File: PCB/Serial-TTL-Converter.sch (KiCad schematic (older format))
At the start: 68 parts, among them J1 RS232 (PC), J2 TTL (uC), J3 power-supply, Q1 BC817, Q2 BC817, Q3 BC817, Q4 BC817, Q5 BC817, Q6 BC817, SW1 SW_SPDT, U1 LT8570, U2 ST75185, U3 MAX736, U4 AP1117-33

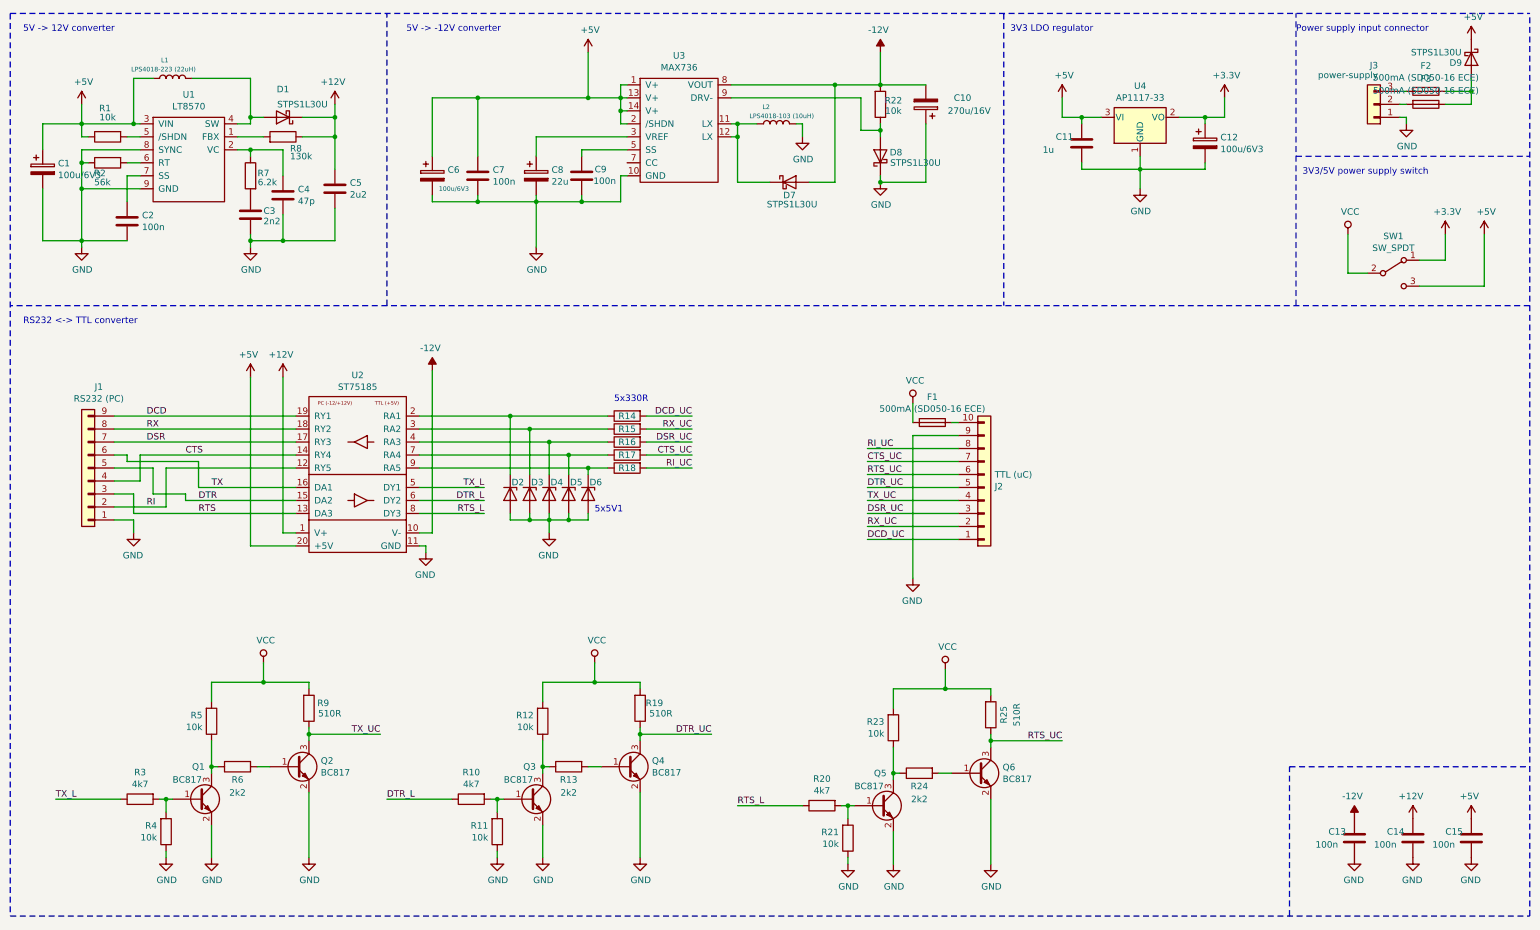
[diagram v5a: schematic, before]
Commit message: Major concept change - use MAX2323 istead of ST75185 (no need power converters)
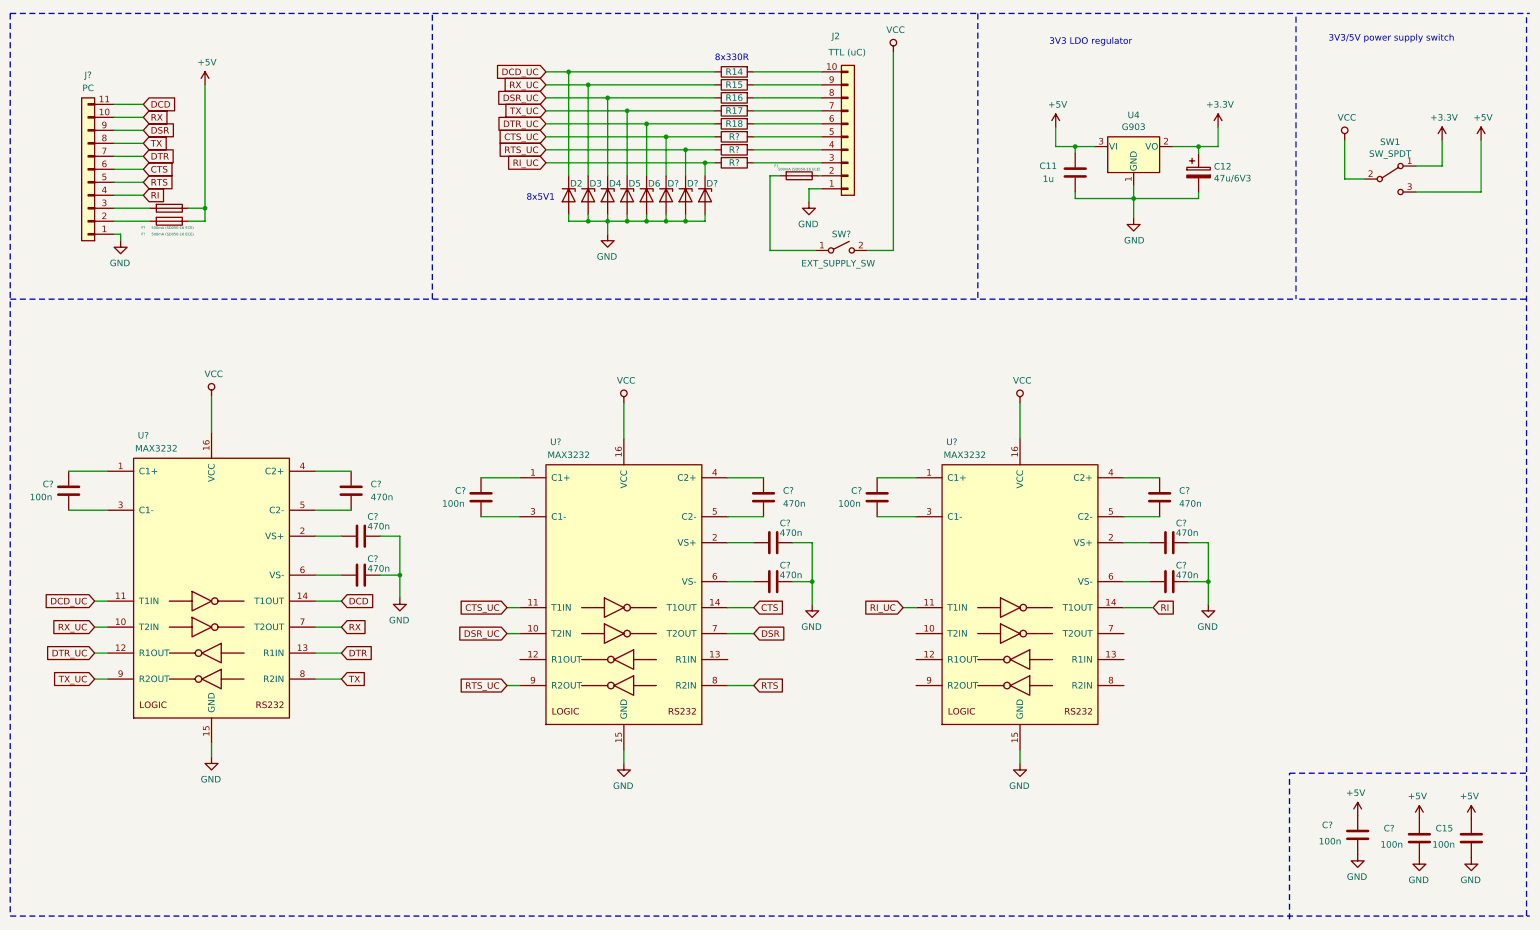
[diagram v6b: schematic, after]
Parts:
- removed C1, C6: 100u/6V3, Capacitor_THT:CP_Radial_D6.3mm_P2.50mm, symbol Device:CP
- removed C10: 270u/16V, Capacitor_THT:CP_Radial_D8.0mm_P3.50mm, symbol Device:CP
- removed C13, C14, C2, C7, C9: 100n, Capacitors_SMD:C_0805, symbol Device:C
- removed C3: 2n2, Capacitors_SMD:C_0805, symbol Device:C
- removed C4: 47p, Capacitors_SMD:C_0805, symbol Device:C
- removed C5: 2u2, Capacitors_SMD:C_0805, symbol Device:C
- removed C8: 22u, Capacitors_Tantalum_SMD:CP_Tantalum_Case-C_EIA-6032-28_Reflow, symbol Device:CP
- removed D1, D7, D8, D9: STPS1L30U, Diodes_SMD:D_SMB, symbol Device:D_Schottky
- removed F2, F3: 500mA (SD050-16 ECE), Fuse:Fuse_1812_4532Metric, symbol Device:Fuse
- removed J1: RS232 (PC), Connectors:1X09_LONGPADS, symbol Connector_Generic:Conn_01x09
- removed J3: power-supply, Connectors:1X03_LONGPADS, symbol Connector_Generic:Conn_01x03
- removed L1: LPS4018-223 (22uH), Inductor_SMD:L_Coilcraft_LPS4018, symbol Device:L
- removed L2: LPS4018-103 (10uH), Inductor_SMD:L_Coilcraft_LPS4018, symbol Device:L
- removed Q1, Q2, Q3, Q4, Q5, Q6: BC817, TO_SOT_Packages_SMD:SOT-23, symbol Transistor_BJT:BC817
- removed R1, R11, R12, R21, R22, R23, R4, R5: 10k, Resistors_SMD:R_0805, symbol Device:R
- removed R10, R20, R3: 4k7, Resistors_SMD:R_0805, symbol Device:R
- removed R13, R24, R6: 2k2, Resistors_SMD:R_0805, symbol Device:R
- removed R19, R25, R9: 510R, Resistors_SMD:R_0805, symbol Device:R
- removed R2: 56k, Resistors_SMD:R_0805, symbol Device:R
- removed R7: 6.2k, Resistors_SMD:R_0805, symbol Device:R
- removed R8: 130k, Resistors_SMD:R_0805, symbol Device:R
- removed U1: LT8570, Housings_SSOP:MSOP-8-1EP_3x3mm_Pitch0.65mm, symbol Serial-TTL-Converter-rescue:LT8570-project-symbols
- removed U2: ST75185, Housings_SOIC:SO-20_12.8x7.5mm_Pitch1.27mm, symbol Serial-TTL-Converter-rescue:ST75185-project-symbols
- removed U3: MAX736, Silicon-Standard:DIP14, symbol Serial-TTL-Converter-rescue:MAX736-project-symbols
- added C? (x5): 100n, Capacitors_SMD:C_0805, symbol Device:C
- added C? (x9): 470n, Capacitors_SMD:C_0805, symbol Device:C
- added D? (x3): 5V1, Diodes_SMD:D_MiniMELF, symbol Device:D_Zener
- added F? (x2): 500mA (SD050-16 ECE), Fuse:Fuse_1812_4532Metric, symbol Device:Fuse
- added J?: PC, symbol Connector_Generic:Conn_01x11
- added R? (x3): 330R, Resistors_SMD:R_0805, symbol Device:R
- added SW?: EXT_SUPPLY_SW, symbol Switch:SW_SPST
- added U? (x3): MAX3232, Housings_SOIC:SOIC-16_3.9x9.9mm_Pitch1.27mm, symbol Interface_UART:MAX3232
- C12: value 100u/6V3 -> 47u/6V3
- U4: value AP1117-33 -> G903; footprint TO_SOT_Packages_SMD:SOT-223 -> TO_SOT_Packages_SMD:SOT-223-3_TabPin2
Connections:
- net +5V: now also C?.1, C?.1, F?.1, F?.1
- net CTS: now also J?.6 (Pin_6), U?.14 (T1OUT)
- net CTS_UC: now also D?.1 (K), R?.1, U?.11 (T1IN); no longer J2.7 (Pin_7), R17.2
- net DCD: now also J?.11 (Pin_11), U?.14 (T1OUT)
- net DCD_UC: now also D2.1 (K), R14.1, U?.11 (T1IN); no longer J2.1 (Pin_1), R14.2
- net DSR: now also J?.9 (Pin_9), U?.7 (T2OUT)
- net DSR_UC: now also D4.1 (K), R16.1, U?.10 (T2IN); no longer J2.3 (Pin_3), R16.2
- net DTR: now also J?.7 (Pin_7), U?.13 (R1IN)
- net DTR_UC: now also D6.1 (K), R18.1, U?.12 (R1OUT); no longer J2.5 (Pin_5)
- net GND: now also J2.1 (Pin_1), C?.1, C?.1, C?.1, C?.1, C?.1, C?.1, C?.2, C?.2, D?.2 (A), D?.2 (A), D?.2 (A), J?.1 (Pin_1), U?.15 (GND), U?.15 (GND), U?.15 (GND); no longer J2.9 (Pin_9)
- net RI: now also J?.4 (Pin_4), U?.14 (T1OUT)
- net RI_UC: now also D?.1 (K), R?.1, U?.11 (T1IN); no longer J2.8 (Pin_8), R18.2
- net RTS: now also J?.5 (Pin_5), U?.8 (R2IN)
- net RTS_UC: now also D?.1 (K), R?.1, U?.9 (R2OUT); no longer J2.6 (Pin_6)
- net RX: now also J?.10 (Pin_10), U?.7 (T2OUT)
- net RX_UC: now also D3.1 (K), R15.1, U?.10 (T2IN); no longer J2.2 (Pin_2), R15.2
- net TX: now also J?.8 (Pin_8), U?.8 (R2IN)
- net TX_UC: now also D5.1 (K), R17.1, U?.9 (R2OUT); no longer J2.4 (Pin_4)
- net VCC: now also SW?.2 (B), U?.16 (VCC), U?.16 (VCC), U?.16 (VCC); no longer F1.2
- net at J2.10 (Pin_10): now also R14.2; no longer F1.1
- new net: F1.1, J2.2 (Pin_2)
- new net: J2.3 (Pin_3), R?.2
- new net: J2.4 (Pin_4), R?.2
- new net: J2.5 (Pin_5), R?.2
- new net: J2.6 (Pin_6), R18.2
- new net: J2.7 (Pin_7), R17.2
- new net: J2.8 (Pin_8), R16.2
- new net: J2.9 (Pin_9), R15.2
- new net: F1.2, SW?.1 (A)
- new net: F?.2, J?.2 (Pin_2)
- new net: F?.2, J?.3 (Pin_3)
- new net: C?.1, U?.1 (C1+) (x3)
- new net: C?.2, U?.2 (VS+) (x3)
- new net: C?.2, U?.3 (C1-) (x3)
- new net: C?.1, U?.4 (C2+) (x3)
- new net: C?.2, U?.5 (C2-) (x3)
- new net: C?.2, U?.6 (VS-) (x3)
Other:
- note added: "8x330R\n"
- note added: "8x5V1"
- note removed: "5V -> -12V converter"
- note removed: "5V -> 12V converter"
- note removed: "5x330R\n"
- note removed: "5x5V1"
- note removed: "Power supply input connector\n"
- note removed: "RS232 <-> TTL converter"
- moved on the sheet: C11, C12, D2, D3, D4, D5, D6, F1, J2, R14, R15, R16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
